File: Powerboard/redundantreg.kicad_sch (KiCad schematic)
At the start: 32 parts

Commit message: removed charger reverse polarity protection
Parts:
- removed Q?: CSD25485F5T-iclr, CSD13385F5, symbol iclr:CSD25485F5T-iclr
- added Q?: CSD25485F5T-iclr, CSD13385F5, symbol iclr:CSD25485F5T-iclr
- gave numbers to parts that had none: 31
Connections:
- net Vout: now also Q?.3
- net at C44.1, C46.1, C49.1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: now also Q?.2
- net at U9.5 (GATE): now also Q?.1
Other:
- note added: "MCH6351"

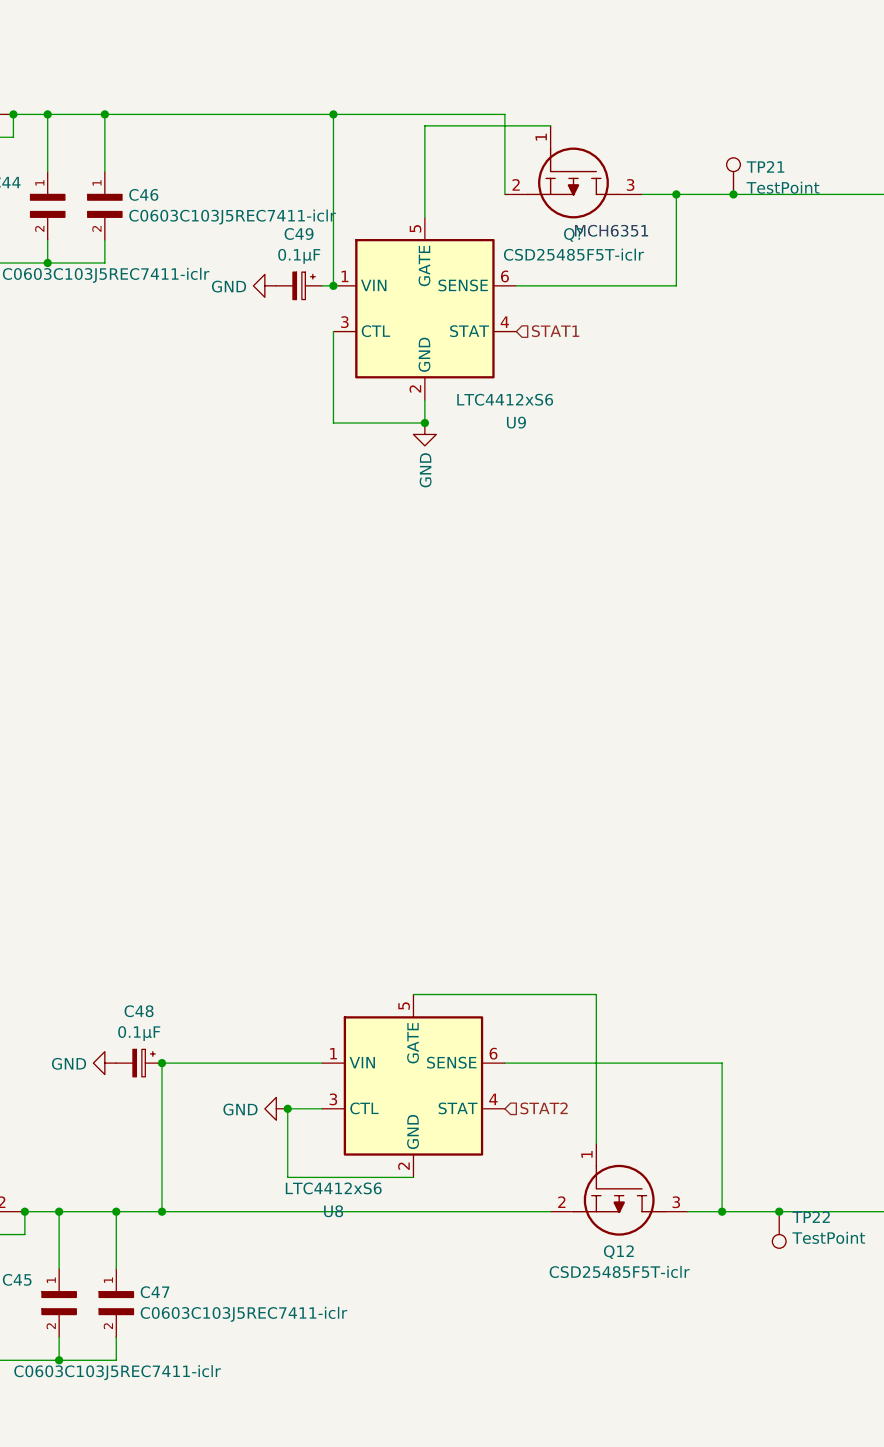
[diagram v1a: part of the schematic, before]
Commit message: changed old mosfets, broke out I2C
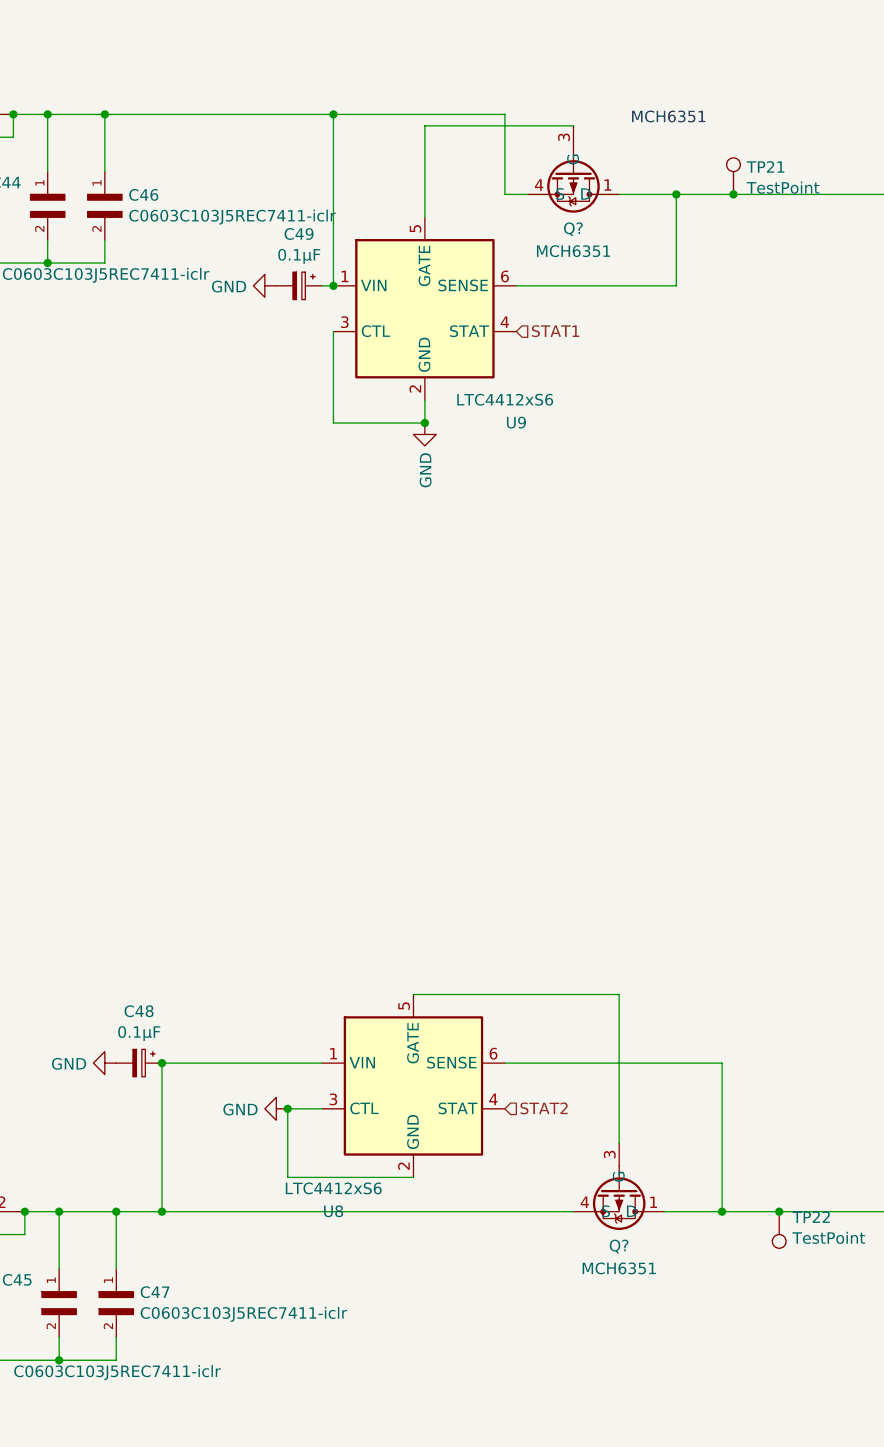
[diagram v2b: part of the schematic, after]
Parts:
- removed Q12, Q?: CSD25485F5T-iclr, CSD13385F5, symbol iclr:CSD25485F5T-iclr
- added Q? (x2): MCH6351, symbol iclr:MCH6351
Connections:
- net Vout: now also Q?.1 (D), Q?.1 (D), Q?.2 (D), Q?.2 (D), Q?.5 (D), Q?.5 (D), Q?.6 (D), Q?.6 (D)
- net at C45.1, C47.1, C48.1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: now also Q?.4 (S)
- net at U8.5 (GATE): now also Q?.3 (G)
- net at C44.1, C46.1, C49.1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: now also Q?.4 (S)
- net at U9.5 (GATE): now also Q?.3 (G)
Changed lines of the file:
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@@
     (stroke (width 0) (type default) (color 0 0 0 0))
   )
-  (wire (pts (xy 224.79 34.29) (xy 228.6 34.29))
+  (wire (pts (xy 222.25 34.29) (xy 228.6 34.29))
     (stroke (width 0) (type default) (color 0 0 0 0))
   )
@@
     (stroke (width 0) (type default) (color 0 0 0 0))
   )
-  (wire (pts (xy 171.45 147.32) (xy 214.63 147.32))
+  (wire (pts (xy 171.45 147.32) (xy 217.17 147.32))
     (stroke (width 0) (type default) (color 0 0 0 0))
   )
@@
     (stroke (width 0) (type default) (color 0 0 0 0))
   )
+  (wire (pts (xy 200.66 26.67) (xy 217.17 26.67))
+    (stroke (width 0) (type default) (color 0 0 0 0))
+  )
   (wire (pts (xy 127 149.86) (xy 156.21 149.86))
     (stroke (width 0) (type default) (color 0 0 0 0))
@@
     (stroke (width 0) (type default) (color 0 0 0 0))
   )
-  (wire (pts (xy 214.63 26.67) (xy 200.66 26.67))
-    (stroke (width 0) (type default) (color 0 0 0 0))
-  )
   (wire (pts (xy 158.75 41.91) (xy 165.1 41.91))
     (stroke (width 0) (type default) (color 0 0 0 0))
@@
     (stroke (width 0) (type default) (color 0 0 0 0))
   )
+  (wire (pts (xy 222.25 123.19) (xy 222.25 139.7))
+    (stroke (width 0) (type default) (color 0 0 0 0))
+  )
   (wire (pts (xy 63.5 151.13) (xy 63.5 147.32))
     (stroke (width 0) (type default) (color 0 0 0 0))
@@
     (stroke (width 0) (type default) (color 0 0 0 0))
   )
-  (wire (pts (xy 199.39 123.19) (xy 219.71 123.19))
+  (wire (pts (xy 199.39 123.19) (xy 222.25 123.19))
     (stroke (width 0) (type default) (color 0 0 0 0))
   )
@@
     (stroke (width 0) (type default) (color 0 0 0 0))
   )
-  (wire (pts (xy 229.87 147.32) (xy 233.68 147.32))
+  (wire (pts (xy 227.33 147.32) (xy 233.68 147.32))
     (stroke (width 0) (type default) (color 0 0 0 0))
   )
@@
     (stroke (width 0) (type default) (color 0 0 0 0))
   )
+  (wire (pts (xy 209.55 34.29) (xy 212.09 34.29))
+    (stroke (width 0) (type default) (color 0 0 0 0))
+  )
   (wire (pts (xy 78.74 163.83) (xy 78.74 166.37))
     (stroke (width 0) (type default) (color 0 0 0 0))
@@
     (stroke (width 0) (type default) (color 0 0 0 0))
   )
-  (wire (pts (xy 219.71 123.19) (xy 219.71 139.7))
-    (stroke (width 0) (type default) (color 0 0 0 0))
-  )
-  (text "MCH6351" (at 217.17 39.37 0)
+  (text "MCH6351" (at 223.52 26.67 0)
     (effects (font (size 1.27 1.27)) (justify left bottom))
   )
@@
     (pin "2")
   )
-  (symbol (lib_id "iclr:CSD25485F5T-iclr") (at 219.71 139.7 270) (unit 1)
-    (in_bom yes) (on_board yes)
-    (property "Reference" "Q12" (id 0) (at 222.25 151.765 90))
-    (property "Value" "CSD25485F5T-iclr" (id 1) (at 222.25 154.0764 90))
-    (property "Footprint" "CSD13385F5" (id 2) (at 218.44 151.13 0)
-      (effects (font (size 1.27 1.27)) (justify left) hide)
-    )
-    (property "Datasheet" "http://www.ti.com/lit/gpn/CSD25485F5" (id 3) (at 215.9 151.13 0)
-      (effects (font (size 1.27 1.27)) (justify left) hide)
-    )
-    (property "Description" "-20V, P ch NexFET MOSFET, single LGA 0.8x1.5, 42mOhm" (id 4) (at 213.36 151.13 0)
-      (effects (font (size 1.27 1.27)) (justify left) hide)
-    )
-    (property "Height" "0" (id 5) (at 210.82 151.13 0)
-      (effects (font (size 1.27 1.27)) (justify left) hide)
-    )
-    (property "Manufacturer_Name" "Texas Instruments" (id 6) (at 208.28 151.13 0)
-      (effects (font (size 1.27 1.27)) (justify left) hide)
-    )
-    (property "Manufacturer_Part_Number" "CSD25485F5T" (id 7) (at 205.74 151.13 0)
-      (effects (font (size 1.27 1.27)) (justify left) hide)
-    )
-    (property "Mouser Part Number" "595-CSD25485F5T" (id 8) (at 203.2 151.13 0)
-      (effects (font (size 1.27 1.27)) (justify left) hide)
-    )
-    (property "Mouser Price/Stock" "https://www.mouser.co.uk/ProductDetail/Texas-Instruments/CSD25485F5T?qs=Bho%2FbeBaDExWIlvMtFx97A%3D%3D" (id 9) (at 200.66 151.13 0)
-      (effects (font (size 1.27 1.27)) (justify left) hide)
-    )
-    (property "Arrow Part Number" "CSD25485F5T" (id 10) (at 198.12 151.13 0)
-      (effects (font (size 1.27 1.27)) (justify left) hide)
-    )
-    (property "Arrow Price/Stock" "https://www.arrow.com/en/products/csd25485f5t/texas-instruments" (id 11) (at 195.58 151.13 0)
-      (effects (font (size 1.27 1.27)) (justify left) hide)
-    )
-    (pin "1")
-    (pin "2")
-    (pin "3")
-  )
   (symbol (lib_id "iclr:C0603C103J5REC7411-iclr") (at 158.75 34.29 270) (unit 1)
     (in_bom yes) (on_board yes)
@@
     (pin "4")
   )
-  (symbol (lib_id "iclr:CSD25485F5T-iclr") (at 214.63 26.67 270) (unit 1)
-    (in_bom yes) (on_board yes)
-    (property "Reference" "Q?" (id 0) (at 217.17 38.735 90))
-    (property "Value" "CSD25485F5T-iclr" (id 1) (at 217.17 41.0464 90))
-    (property "Footprint" "CSD13385F5" (id 2) (at 213.36 38.1 0)
-      (effects (font (size 1.27 1.27)) (justify left) hide)
-    )
-    (property "Datasheet" "http://www.ti.com/lit/gpn/CSD25485F5" (id 3) (at 210.82 38.1 0)
-      (effects (font (size 1.27 1.27)) (justify left) hide)
-    )
-    (property "Description" "-20V, P ch NexFET MOSFET, single LGA 0.8x1.5, 42mOhm" (id 4) (at 208.28 38.1 0)
-      (effects (font (size 1.27 1.27)) (justify left) hide)
-    )
-    (property "Height" "0" (id 5) (at 205.74 38.1 0)
-      (effects (font (size 1.27 1.27)) (justify left) hide)
-    )
-    (property "Manufacturer_Name" "Texas Instruments" (id 6) (at 203.2 38.1 0)
-      (effects (font (size 1.27 1.27)) (justify left) hide)
-    )
-    (property "Manufacturer_Part_Number" "CSD25485F5T" (id 7) (at 200.66 38.1 0)
-      (effects (font (size 1.27 1.27)) (justify left) hide)
-    )
-    (property "Mouser Part Number" "595-CSD25485F5T" (id 8) (at 198.12 38.1 0)
-      (effects (font (size 1.27 1.27)) (justify left) hide)
-    )
-    (property "Mouser Price/Stock" "https://www.mouser.co.uk/ProductDetail/Texas-Instruments/CSD25485F5T?qs=Bho%2FbeBaDExWIlvMtFx97A%3D%3D" (id 9) (at 195.58 38.1 0)
-      (effects (font (size 1.27 1.27)) (justify left) hide)
-    )
-    (property "Arrow Part Number" "CSD25485F5T" (id 10) (at 193.04 38.1 0)
-      (effects (font (size 1.27 1.27)) (justify left) hide)
-    )
-    (property "Arrow Price/Stock" "https://www.arrow.com/en/products/csd25485f5t/texas-instruments" (id 11) (at 190.5 38.1 0)
-      (effects (font (size 1.27 1.27)) (justify left) hide)
+  (symbol (lib_id "iclr:MCH6351") (at 236.22 22.86 270) (unit 1)
+    (in_bom yes) (on_board yes)
+    (property "Reference" "Q?" (id 0) (at 217.17 38.1 90))
+    (property "Value" "MCH6351" (id 1) (at 217.17 40.64 90))
+    (property "Footprint" "" (id 2) (at 218.44 38.1 0)
+      (effects (font (size 1.27 1.27)) hide)
+    )
+    (property "Datasheet" "" (id 3) (at 218.44 38.1 0)
+      (effects (font (size 1.27 1.27)) hide)
     )
     (pin "1")
     (pin "2")
     (pin "3")
+    (pin "4")
+    (pin "5")
+    (pin "6")
+  )
+  (symbol (lib_id "iclr:MCH6351") (at 241.3 135.89 270) (unit 1)
+    (in_bom yes) (on_board yes)
+    (property "Reference" "Q?" (id 0) (at 222.25 151.13 90))
+    (property "Value" "MCH6351" (id 1) (at 222.25 153.67 90))
+    (property "Footprint" "" (id 2) (at 223.52 151.13 0)
+      (effects (font (size 1.27 1.27)) hide)
+    )
+    (property "Datasheet" "" (id 3) (at 223.52 151.13 0)
+      (effects (font (size 1.27 1.27)) hide)
+    )
+    (pin "1")
+    (pin "2")
+    (pin "3")
+    (pin "4")
+    (pin "5")
+    (pin "6")
   )
 )

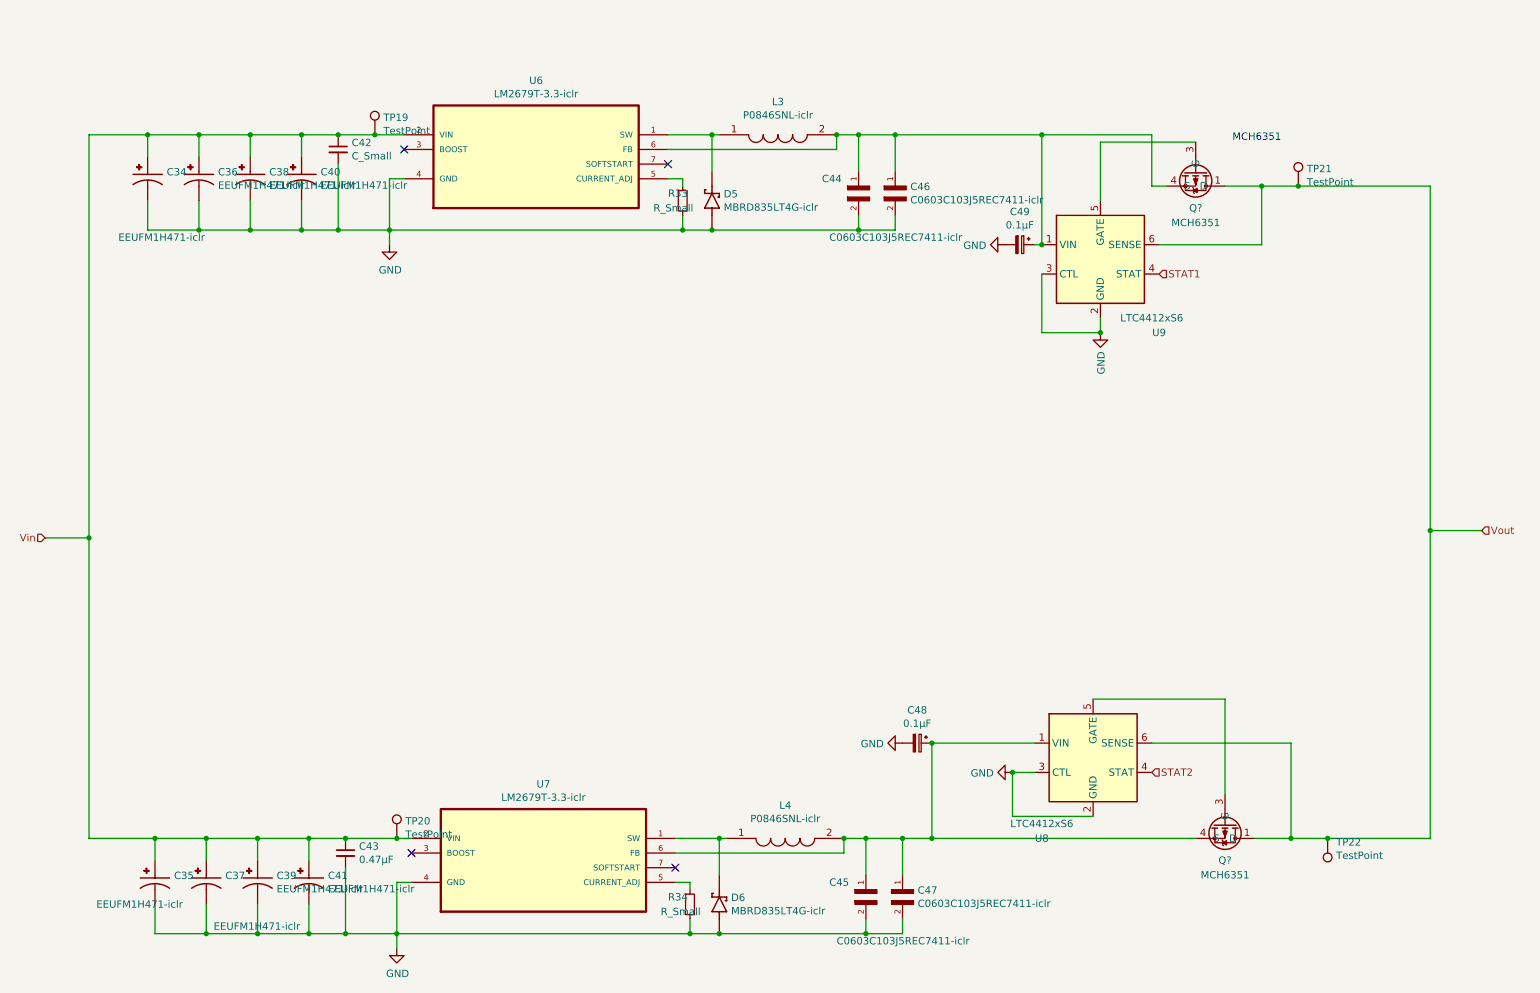
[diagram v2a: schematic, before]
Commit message: 3v3 reg cap & inductor changes, added boost capacitor
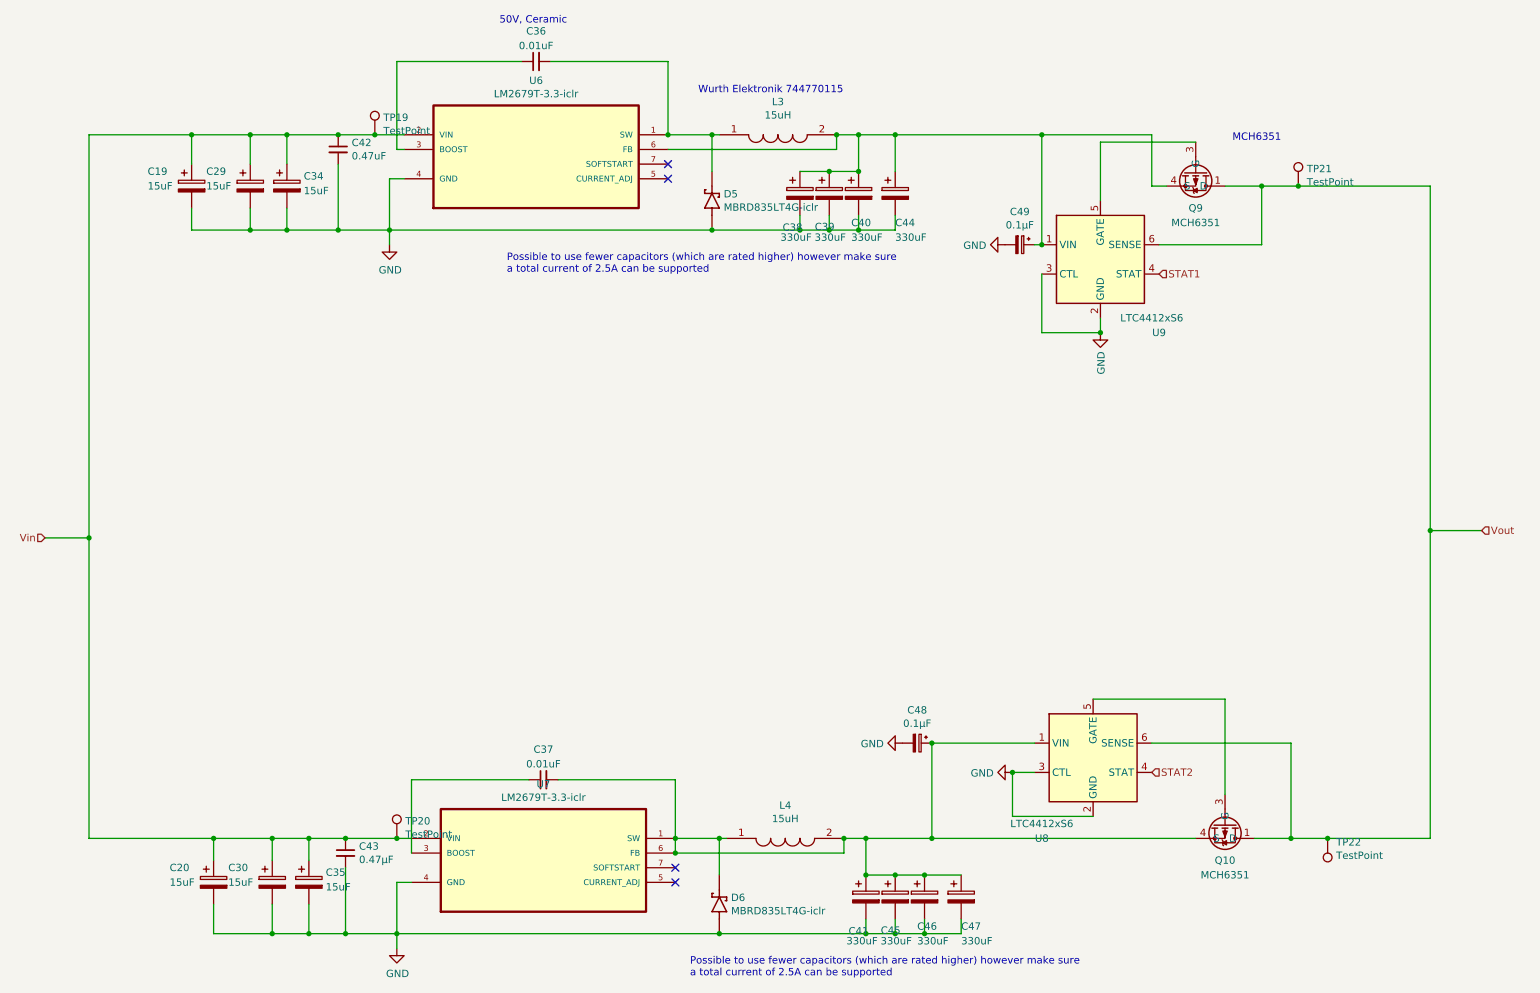
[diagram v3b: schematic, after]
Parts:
- removed C34, C35, C36, C37, C38, C39, C40, C41: EEUFM1H471-iclr, CAPPRD500W60D1250H2000, symbol iclr:EEUFM1H471-iclr
- removed C44, C45, C46, C47: C0603C103J5REC7411-iclr, CAPC1608X87N, symbol iclr:C0603C103J5REC7411-iclr
- removed R33, R34: R_Small, symbol Device:R_Small
- added C19, C20, C29, C30, C34, C35: 15uF, symbol Device:C_Polarized
- added C36, C37: 0.01uF, symbol Device:C_Small
- added C38, C39, C40, C41, C44, C45, C46, C47: 330uF, symbol Device:C_Polarized
- C42: value C_Small -> 0.47uF
- L3, L4: value P0846SNL-iclr -> 15uH
- TP19, TP20, TP21, TP22: footprint (none) -> TestPoint:TestPoint_Pad_D1.0mm
- gave numbers to parts that had none: 2
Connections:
- net GND: now also C19.2, C20.2, C29.2, C30.2, C34.2, C35.2, C38.2, C39.2, C40.2, C41.2, C44.2, C45.2, C46.2, C47.2
- net Vin: now also C19.1, C20.1, C29.1, C30.1, C34.1, C35.1
- net at C48.1, L4.2, Q10.4 (S)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: now also D6.4, L4.1, U7.1 (SW), C37.2, C41.1, C45.1, C46.1, C47.1
- net at C49.1, L3.2, Q9.4 (S)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: now also C38.1, C39.1, C40.1, C44.1
- net at D5.4, L3.1, U6.1 (SW): now also C36.2
- net at U6.3 (BOOST): now also C36.1
- net at U7.3 (BOOST): now also C37.1
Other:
- note added: "50V, Ceramic"
- note added: "Possible to use fewer capacitors (which are rated higher) however make sure a total current of 2.5A can be supported"
- note added: "Wurth Elektronik 744770115"
